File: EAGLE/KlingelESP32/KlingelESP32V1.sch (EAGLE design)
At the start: 29 parts, among them IC1 ESP-12E/F, J1 796683-2, J2 796683-2, J3 796683-2, J4 796683-2, Q1 AO3401

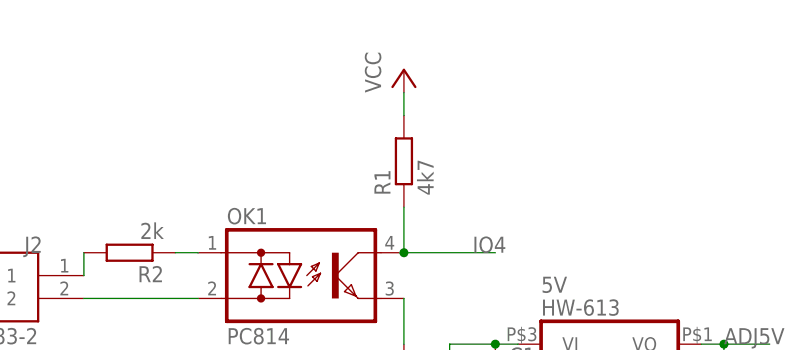
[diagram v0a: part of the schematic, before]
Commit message: Another error in VCC usage...
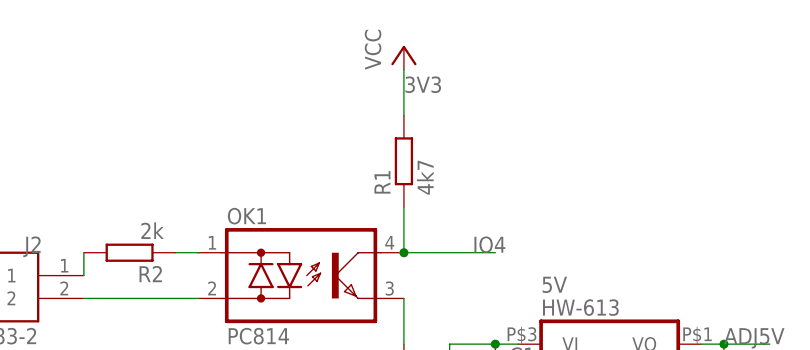
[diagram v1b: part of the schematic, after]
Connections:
- removed net VCC: R1.2
- net 3V3: now also R1.2
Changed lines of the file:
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@@
 <attribute name="VALUE" x="-60.96" y="25.4" size="1.778" layer="96"/>
 </instance>
-<instance part="P+3" gate="VCC" x="17.78" y="160.02" smashed="yes">
-<attribute name="VALUE" x="15.24" y="157.48" size="1.778" layer="96" rot="R90"/>
+<instance part="P+3" gate="VCC" x="17.78" y="162.56" smashed="yes">
+<attribute name="VALUE" x="15.24" y="160.02" size="1.778" layer="96" rot="R90"/>
 </instance>
 <instance part="R1" gate="G$1" x="17.78" y="149.86" smashed="yes" rot="R90">
@@
 <label x="88.9" y="119.38" size="1.778" layer="95"/>
 </segment>
+<segment>
+<pinref part="P+3" gate="VCC" pin="VCC"/>
+<pinref part="R1" gate="G$1" pin="2"/>
+<wire x1="17.78" y1="160.02" x2="17.78" y2="154.94" width="0.1524" layer="91"/>
+<label x="17.78" y="157.48" size="1.778" layer="95"/>
+</segment>
 </net>
 <net name="RST" class="0">
@@
 </segment>
 </net>
-<net name="VCC" class="0">
-<segment>
-<pinref part="P+3" gate="VCC" pin="VCC"/>
-<pinref part="R1" gate="G$1" pin="2"/>
-<wire x1="17.78" y1="157.48" x2="17.78" y2="154.94" width="0.1524" layer="91"/>
-</segment>
-</net>
